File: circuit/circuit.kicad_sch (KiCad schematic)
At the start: 14 parts, among them J1 POWER, J2 BLUETOOTH, J3 BUZZER, SW1 SW_Push, U1 ADXL359

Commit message: pcb v2.1
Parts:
- added R1: R, Resistor_SMD:R_1206_3216Metric_Pad1.30x1.75mm_HandSolder, symbol pspice:R
- added SW2: SW_DPDT_x2, Connector_PinSocket_2.00mm:PinSocket_1x03_P2.00mm_Vertical, symbol Switch:SW_DPDT_x2
- J1: footprint Connector_PinSocket_1.00mm:PinSocket_1x02_P1.00mm_Vertical -> Connector_PinSocket_2.00mm:PinSocket_1x02_P2.00mm_Vertical
- J2: footprint Connector_PinSocket_1.00mm:PinSocket_1x04_P1.00mm_Vertical -> Connector_PinSocket_2.00mm:PinSocket_1x04_P2.00mm_Vertical
- J3: footprint Connector_PinSocket_1.00mm:PinSocket_1x03_P1.00mm_Vertical -> Connector_PinSocket_2.00mm:PinSocket_1x03_P2.00mm_Vertical
- SW1: footprint Button_Switch_THT:SW_PUSH_6mm -> lowprint-pcb-ee410:sw_push_5mm
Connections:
- net GND: now also R1.2
- net 9V: no longer names the net of J1.2 (Pin_2)
- net 9V: now also SW2.2 (B); no longer A1.30 (VIN)
- new net Vin: A1.30 (VIN), R1.1, SW2.3 (C)
- no-connect marks 22 -> 23
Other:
- moved on the sheet: J1

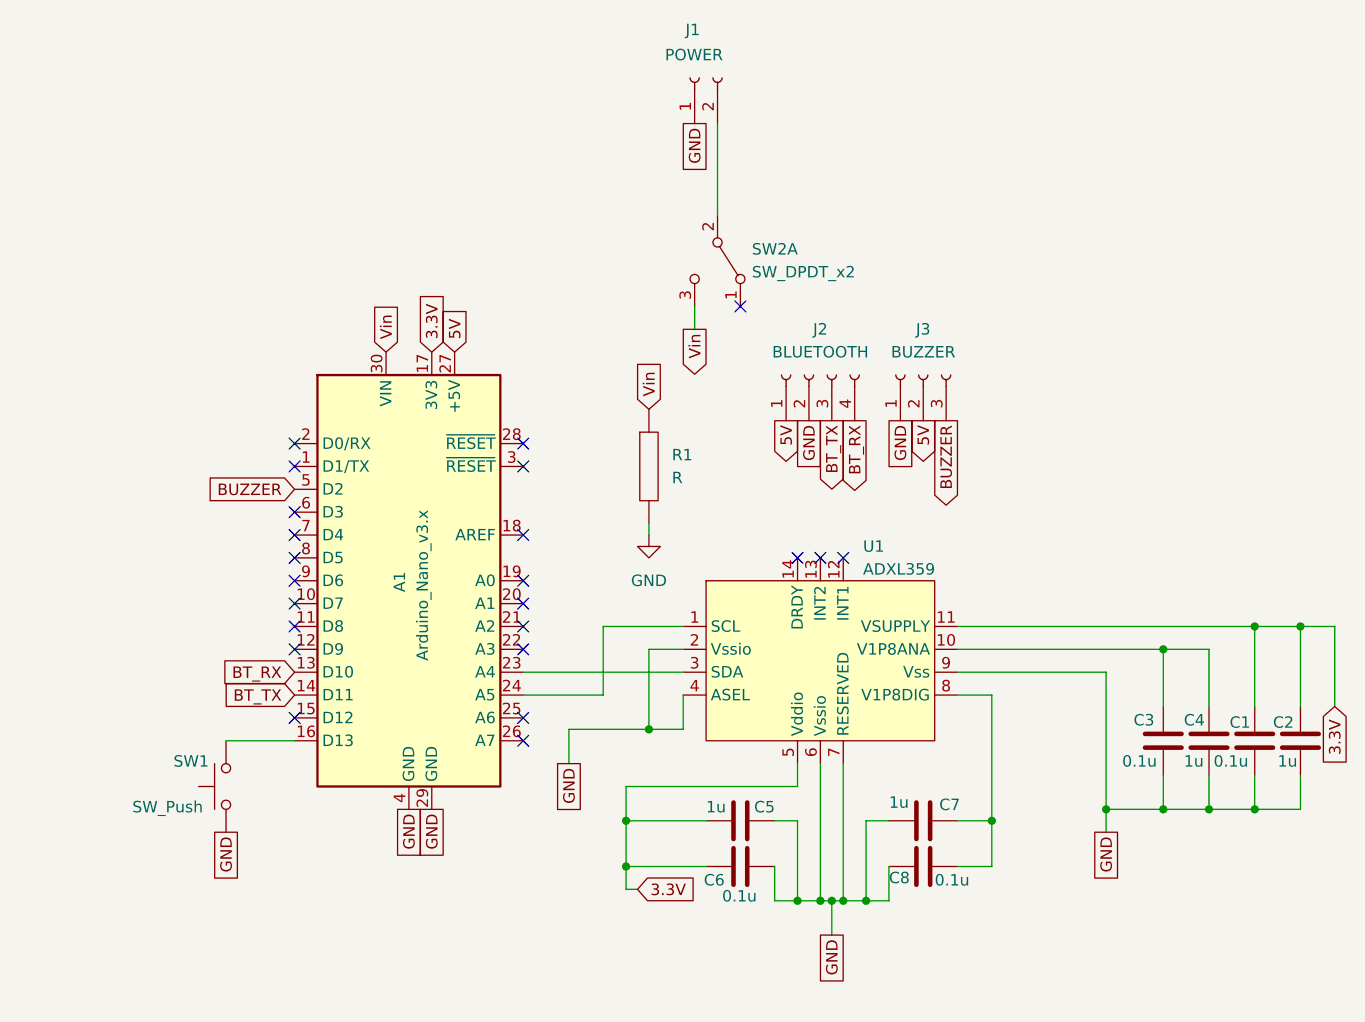
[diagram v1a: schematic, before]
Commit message: Work PCB
Small Fix on PCB
+ Solve error on the resistance for the button (pcb)
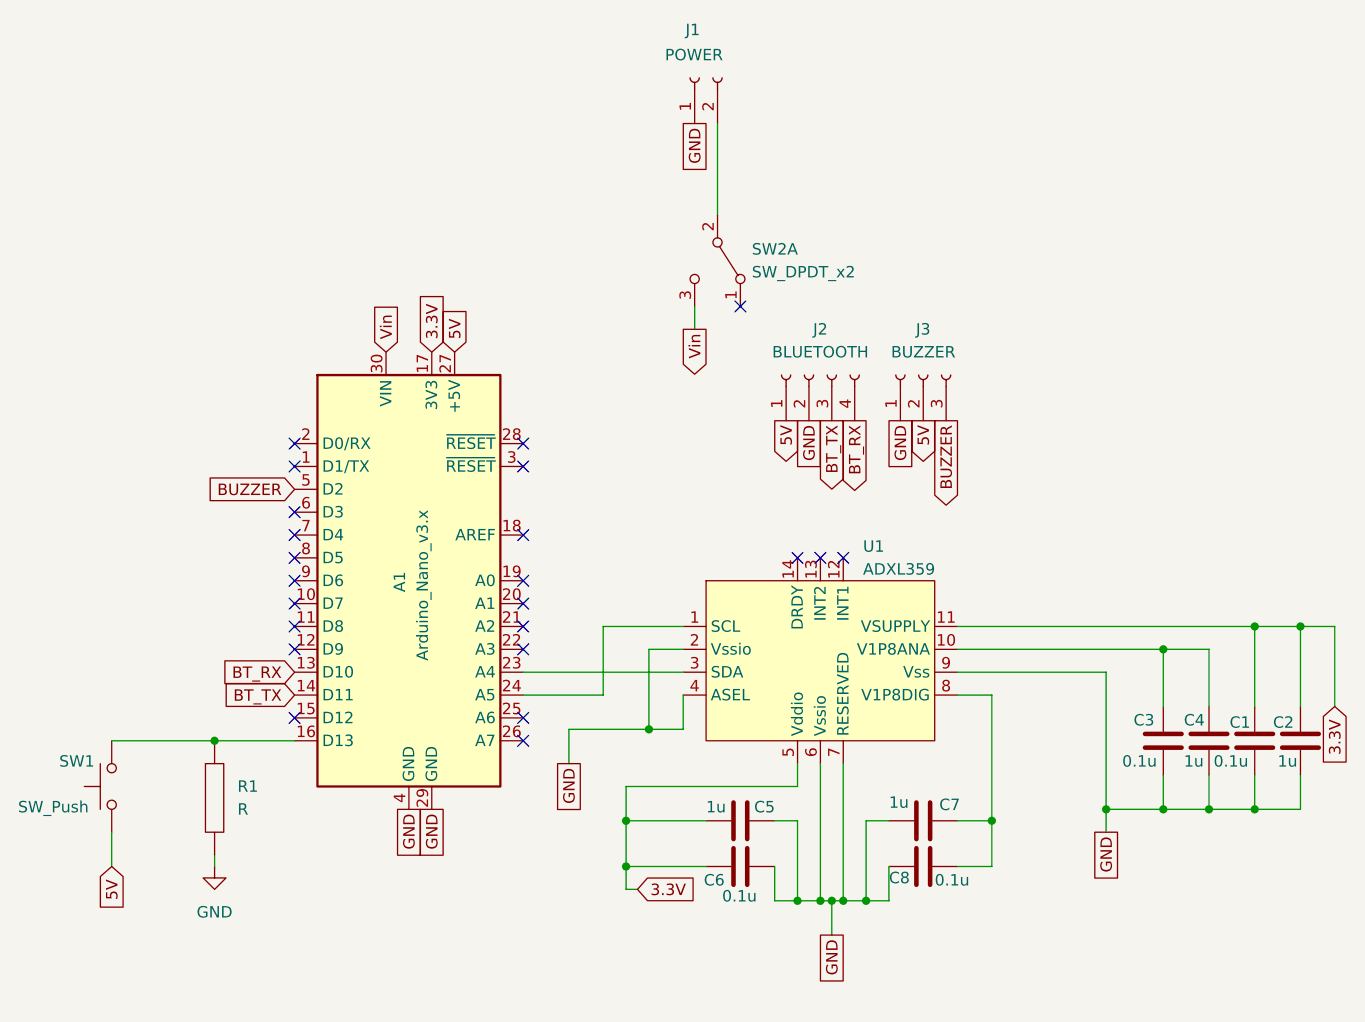
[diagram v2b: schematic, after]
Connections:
- net 5V: now also SW1.1
- net GND: no longer SW1.1
- net Vin: no longer R1.1
- net at A1.16 (D13), SW1.2: now also R1.1
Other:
- moved on the sheet: R1, SW1
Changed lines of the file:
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@@
+	)
+	(junction
+		(at 88.9 115.57)
+		(diameter 0)
+		(color 0 0 0 0)
 	)
 	(junction
@@
 	(wire
 		(pts
+			(xy 77.47 125.73) (xy 77.47 129.54)
+		)
+		(stroke
+			(width 0)
+			(type default)
+		)
+	)
+	(wire
+		(pts
 			(xy 194.31 119.38) (xy 194.31 123.19)
 		)
@@
 	(wire
 		(pts
+			(xy 88.9 115.57) (xy 97.79 115.57)
+		)
+		(stroke
+			(width 0)
+			(type default)
+		)
+	)
+	(wire
+		(pts
 			(xy 157.48 133.35) (xy 156.21 133.35)
 		)
@@
 	(wire
 		(pts
-			(xy 90.17 115.57) (xy 97.79 115.57)
+			(xy 77.47 115.57) (xy 88.9 115.57)
 		)
 		(stroke
@@
 	(wire
 		(pts
-			(xy 137.16 91.44) (xy 137.16 92.71)
+			(xy 88.9 128.27) (xy 88.9 129.54)
 		)
 		(stroke
@@
 		)
 	)
-	(global_label "GND"
-		(shape passive)
-		(at 90.17 125.73 270)
+	(global_label "5V"
+		(shape input)
+		(at 77.47 129.54 270)
 		(fields_autoplaced yes)
 		(effects
@@
 		)
 		(property "Intersheetrefs" "${INTERSHEET_REFS}"
-			(at 90.17 131.4744 90)
+			(at 77.47 134.8233 90)
 			(effects
 				(font
@@
 				)
 				(justify right)
-				(hide yes)
-			)
-		)
-	)
-	(global_label "Vin"
-		(shape input)
-		(at 137.16 78.74 90)
-		(fields_autoplaced yes)
-		(effects
-			(font
-				(size 1.27 1.27)
-			)
-			(justify left)
-		)
-		(property "Intersheetrefs" "${INTERSHEET_REFS}"
-			(at 137.16 72.9124 90)
-			(effects
-				(font
-					(size 1.27 1.27)
-				)
-				(justify left)
 				(hide yes)
 			)
@@
 	(symbol
 		(lib_id "power:GND")
-		(at 137.16 92.71 0)
+		(at 88.9 129.54 0)
 		(unit 1)
 		(exclude_from_sim no)
@@
 		(fields_autoplaced yes)
 		(property "Reference" "#PWR01"
-			(at 137.16 99.06 0)
+			(at 88.9 135.89 0)
 			(effects
 				(font
@@
 		)
 		(property "Value" "GND"
-			(at 137.16 97.79 0)
+			(at 88.9 134.62 0)
 			(effects
 				(font
@@
 		)
 		(property "Footprint" ""
-			(at 137.16 92.71 0)
+			(at 88.9 129.54 0)
 			(effects
 				(font
@@
 		)
 		(property "Datasheet" ""
-			(at 137.16 92.71 0)
+			(at 88.9 129.54 0)
 			(effects
 				(font
@@
 		)
 		(property "Description" "Power symbol creates a global label with name \"GND\" , ground"
-			(at 137.16 92.71 0)
+			(at 88.9 129.54 0)
 			(effects
 				(font
@@
 		)
 		(instances
-			(project ""
+			(project "circuit"
 				(path "/1f28986f-6d6b-4631-9eb2-ab0a7fc03bc3"
 					(reference "#PWR01")
@@
 		)
 		(instances
-			(project ""
+			(project "circuit"
 				(path "/1f28986f-6d6b-4631-9eb2-ab0a7fc03bc3"
 					(reference "J3")
@@
 		)
 		(instances
-			(project ""
+			(project "circuit"
 				(path "/1f28986f-6d6b-4631-9eb2-ab0a7fc03bc3"
 					(reference "J1")
@@
 		)
 		(instances
-			(project ""
+			(project "circuit"
 				(path "/1f28986f-6d6b-4631-9eb2-ab0a7fc03bc3"
 					(reference "A1")
@@
 		)
 		(instances
-			(project ""
+			(project "circuit"
 				(path "/1f28986f-6d6b-4631-9eb2-ab0a7fc03bc3"
 					(reference "J2")
@@
 	(symbol
 		(lib_id "pspice:R")
-		(at 137.16 85.09 0)
+		(at 88.9 121.92 0)
 		(unit 1)
 		(exclude_from_sim no)
@@
 		(fields_autoplaced yes)
 		(property "Reference" "R1"
-			(at 139.7 83.8199 0)
+			(at 91.44 120.6499 0)
 			(effects
 				(font
@@
 		)
 		(property "Value" "R"
-			(at 139.7 86.3599 0)
+			(at 91.44 123.1899 0)
 			(effects
 				(font
@@
 		)
 		(property "Footprint" "Resistor_SMD:R_1206_3216Metric_Pad1.30x1.75mm_HandSolder"
-			(at 137.16 85.09 0)
+			(at 88.9 121.92 0)
 			(effects
 				(font
@@
 		)
 		(property "Datasheet" "~"
-			(at 137.16 85.09 0)
+			(at 88.9 121.92 0)
 			(effects
 				(font
@@
 		)
 		(property "Description" "Resistor symbol for simulation only"
-			(at 137.16 85.09 0)
+			(at 88.9 121.92 0)
 			(effects
 				(font
@@
 		)
 		(instances
-			(project ""
+			(project "circuit"
 				(path "/1f28986f-6d6b-4631-9eb2-ab0a7fc03bc3"
 					(reference "R1")
@@
 	(symbol
 		(lib_id "Switch:SW_Push")
-		(at 90.17 120.65 90)
+		(at 77.47 120.65 90)
 		(unit 1)
 		(exclude_from_sim no)
@@
 		(dnp no)
 		(property "Reference" "SW1"
-			(at 84.328 117.856 90)
+			(at 71.628 117.856 90)
 			(effects
 				(font
@@
 		)
 		(property "Value" "SW_Push"
-			(at 79.756 122.936 90)
+			(at 67.056 122.936 90)
 			(effects
 				(font
@@
 		)
 		(property "Footprint" "lowprint-pcb-ee410:sw_push_5mm"
-			(at 85.09 120.65 0)
+			(at 72.39 120.65 0)
 			(effects
 				(font
@@
 		)
 		(property "Datasheet" "~"
-			(at 85.09 120.65 0)
+			(at 72.39 120.65 0)
 			(effects
 				(font
@@
 		)
 		(property "Description" "Push button switch, generic, two pins"
-			(at 90.17 120.65 0)
+			(at 77.47 120.65 0)
 			(effects
 				(font
@@
 		)
 		(instances
-			(project ""
+			(project "circuit"
 				(path "/1f28986f-6d6b-4631-9eb2-ab0a7fc03bc3"
 					(reference "SW1")
@@
 		)
 		(instances
-			(project ""
+			(project "circuit"
 				(path "/1f28986f-6d6b-4631-9eb2-ab0a7fc03bc3"
 					(reference "C1")
@@
 		)
 		(instances
-			(project ""
+			(project "circuit"
 				(path "/1f28986f-6d6b-4631-9eb2-ab0a7fc03bc3"
 					(reference "SW2")
@@
 		)
 		(instances
-			(project ""
+			(project "circuit"
 				(path "/1f28986f-6d6b-4631-9eb2-ab0a7fc03bc3"
 					(reference "U1")
